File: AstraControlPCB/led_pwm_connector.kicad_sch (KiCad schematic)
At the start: 11 parts, among them CN7 JST_VH_8PIN_10A_250V

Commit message: Update wks file
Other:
- company: (none) -> LiveAstra Technologies
- title: PWM Connector -> AstraControl - Root
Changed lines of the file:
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@@
 	(paper "A4")
 	(title_block
-		(title "PWM Connector")
+		(title "AstraControl - Root")
+		(date "2024-08-26")
+		(rev "A")
+		(company "LiveAstra Technologies")
 	)
 	(junction
@@
 		(effects
 			(font
-				(face "Sarabun")
+				(face "ING Me")
 				(size 3 3)
 				(color 255 255 255 1)
@@
 		(effects
 			(font
-				(face "Sarabun")
+				(face "ING Me")
 				(size 1.5 1.5)
 				(color 255 255 255 1)

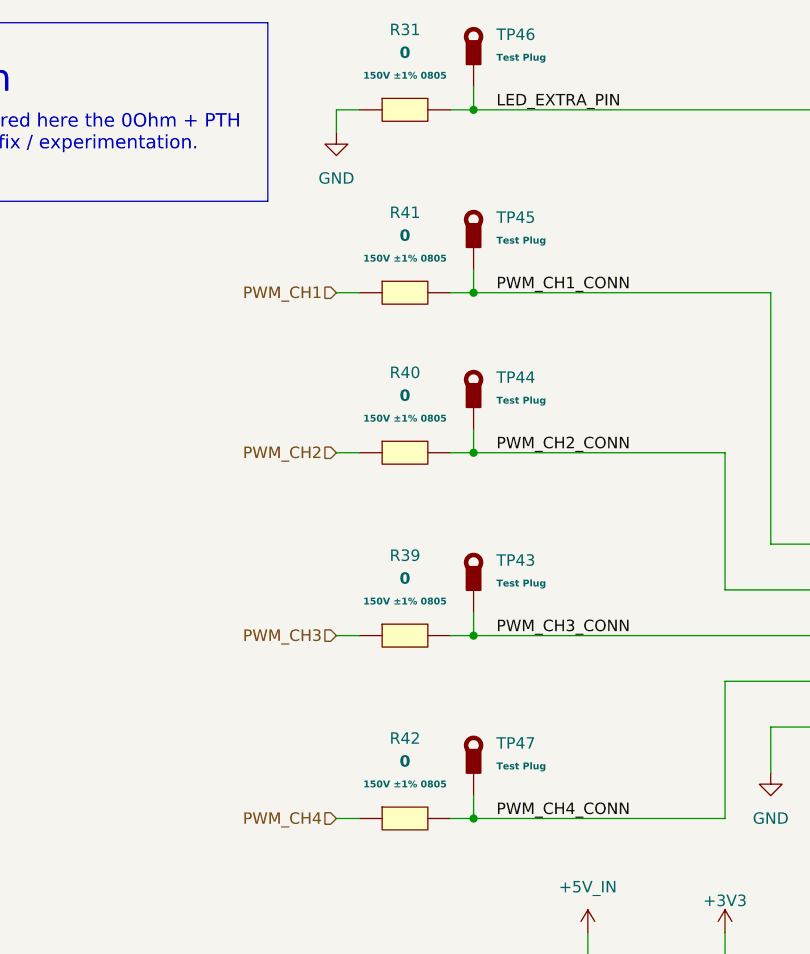
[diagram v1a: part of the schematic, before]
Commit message: Remove plus minus symbol
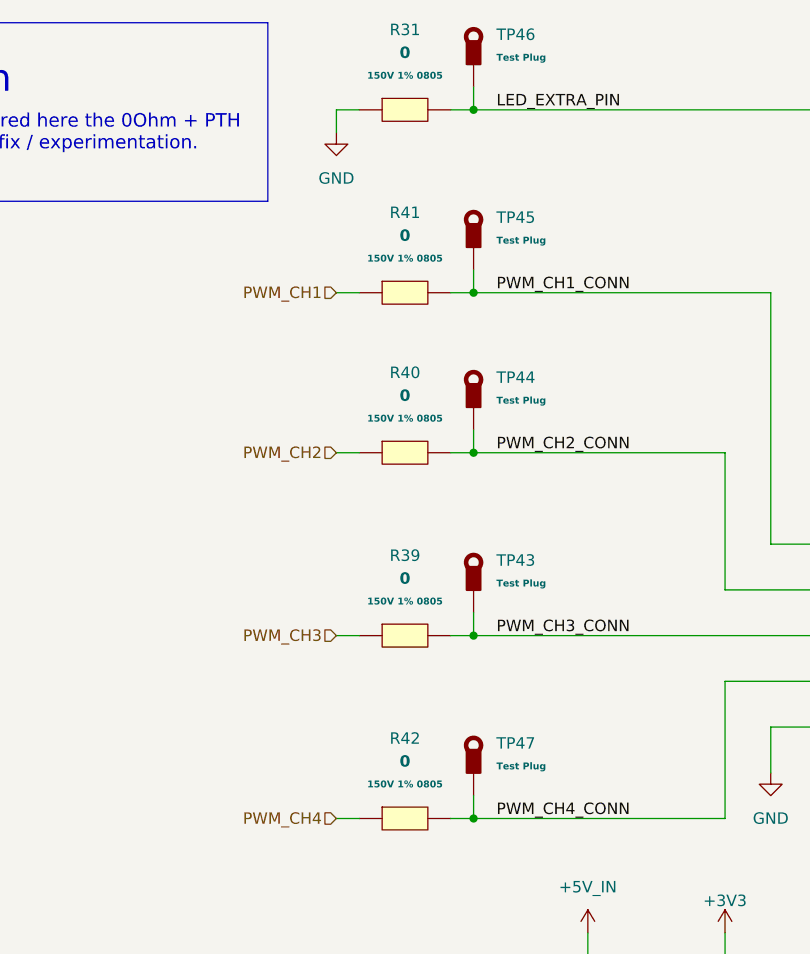
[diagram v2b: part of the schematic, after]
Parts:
- R31, R39, R40, R41, R42: Extra Values 150V ±1% 0805 -> 150V 1% 0805
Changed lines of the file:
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@@
-			)
-		)
-		(property "Extra Value" ""
-			(at 182.88 96.52 0)
-			(effects
-				(font
-					(size 1.27 1.27)
-				)
-				(hide yes)
 			)
 		)
@@
 			)
 		)
-		(property "Extra Value" ""
-			(at 124.46 53.34 0)
-			(effects
-				(font
-					(size 1.27 1.27)
-				)
-				(hide yes)
-			)
-		)
 		(pin "1"
 		)
@@
 		(dnp no)
 		(fields_autoplaced yes)
-		(property "Reference" "#PWR074"
+		(property "Reference" "#PWR74"
 			(at 137.16 130.81 0)
 			(effects
@@
 			(project "AstraControl"
 				(path "/9a751838-dce8-4d69-8a02-736625ac74e7/0db21d8e-3390-4d67-877f-0e5d98e37848/e7f4ae23-1ac9-4fa3-959c-a78f85f3f546"
-					(reference "#PWR074")
+					(reference "#PWR74")
 					(unit 1)
 				)
@@
 		(on_board yes)
 		(dnp no)
-		(property "Reference" "#PWR073"
+		(property "Reference" "#PWR73"
 			(at 152.4 130.81 0)
 			(effects
@@
 			(project "AstraControl"
 				(path "/9a751838-dce8-4d69-8a02-736625ac74e7/0db21d8e-3390-4d67-877f-0e5d98e37848/e7f4ae23-1ac9-4fa3-959c-a78f85f3f546"
-					(reference "#PWR073")
+					(reference "#PWR73")
 					(unit 1)
 				)
@@
 			)
 		)
-		(property "Extra Values" "150V ±1% 0805"
+		(property "Extra Values" "150V 1% 0805"
 			(at 116.84 31.75 0)
 			(effects
@@
 					(bold yes)
 				)
-			)
-		)
-		(property "Extra Value" ""
-			(at 116.84 35.56 0)
-			(effects
-				(font
-					(size 1.27 1.27)
-				)
-				(hide yes)
 			)
 		)
@@
 		(dnp no)
 		(fields_autoplaced yes)
-		(property "Reference" "#PWR075"
+		(property "Reference" "#PWR75"
 			(at 157.48 115.57 0)
 			(effects
@@
 			(project "AstraControl"
 				(path "/9a751838-dce8-4d69-8a02-736625ac74e7/0db21d8e-3390-4d67-877f-0e5d98e37848/e7f4ae23-1ac9-4fa3-959c-a78f85f3f546"
-					(reference "#PWR075")
+					(reference "#PWR75")
 					(unit 1)
 				)
@@
 			)
 		)
-		(property "Extra Values" "150V ±1% 0805"
+		(property "Extra Values" "150V 1% 0805"
 			(at 116.84 69.85 0)
 			(effects
@@
 					(bold yes)
 				)
-			)
-		)
-		(property "Extra Value" ""
-			(at 116.84 73.66 0)
-			(effects
-				(font
-					(size 1.27 1.27)
-				)
-				(hide yes)
 			)
 		)
@@
 			)
 		)
-		(property "Extra Value" ""
-			(at 124.46 71.12 0)
-			(effects
-				(font
-					(size 1.27 1.27)
-				)
-				(hide yes)
-			)
-		)
 		(pin "1"
 		)
@@
 			)
 		)
-		(property "Extra Values" "150V ±1% 0805"
+		(property "Extra Values" "150V 1% 0805"
 			(at 116.84 52.07 0)
 			(effects
@@
 					(bold yes)
 				)
-			)
-		)
-		(property "Extra Value" ""
-			(at 116.84 55.88 0)
-			(effects
-				(font
-					(size 1.27 1.27)
-				)
-				(hide yes)
 			)
 		)
@@
 		(dnp no)
 		(fields_autoplaced yes)
-		(property "Reference" "#PWR072"
+		(property "Reference" "#PWR72"
 			(at 109.22 44.45 0)
 			(effects
@@
 			(project "AstraControl"
 				(path "/9a751838-dce8-4d69-8a02-736625ac74e7/0db21d8e-3390-4d67-877f-0e5d98e37848/e7f4ae23-1ac9-4fa3-959c-a78f85f3f546"
-					(reference "#PWR072")
+					(reference "#PWR72")
 					(unit 1)
 				)
@@
 			)
 		)
-		(property "Extra Value" ""
-			(at 124.46 111.76 0)
-			(effects
-				(font
-					(size 1.27 1.27)
-				)
-				(hide yes)
-			)
-		)
 		(pin "1"
 		)
@@
 			)
 		)
-		(property "Extra Value" ""
-			(at 124.46 91.44 0)
-			(effects
-				(font
-					(size 1.27 1.27)
-				)
-				(hide yes)
-			)
-		)
 		(pin "1"
 		)
@@
 			)
 		)
-		(property "Extra Values" "150V ±1% 0805"
+		(property "Extra Values" "150V 1% 0805"
 			(at 116.84 110.49 0)
 			(effects
@@
 					(bold yes)
 				)
-			)
-		)
-		(property "Extra Value" ""
-			(at 116.84 114.3 0)
-			(effects
-				(font
-					(size 1.27 1.27)
-				)
-				(hide yes)
 			)
 		)
@@
 			)
 		)
-		(property "Extra Values" "150V ±1% 0805"
+		(property "Extra Values" "150V 1% 0805"
 			(at 116.84 90.17 0)
 			(effects
@@
 					(bold yes)
 				)
-			)
-		)
-		(property "Extra Value" ""
-			(at 116.84 93.98 0)
-			(effects
-				(font
-					(size 1.27 1.27)
-				)
-				(hide yes)
 			)
 		)
@@
 			)
 		)
-		(property "Extra Value" ""
-			(at 124.46 33.02 0)
-			(effects
-				(font
-					(size 1.27 1.27)
-				)
-				(hide yes)
-			)
-		)

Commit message: workflow
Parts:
- added INF5: ~, symbol LiveAstra:Information_Box
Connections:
- net LED_EXTRA_PIN renamed EXTRA_PIN
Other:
- note added: "PWM Connector"
- note removed: "If a different signal is required here the 0Ohm + PTH will allow a post assembly fix / experimentation. Otherwise, just GND."
- note removed: "Information"
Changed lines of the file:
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@@
 		)
 	)
-	(rectangle
-		(start 41.7033 25.88)
-		(end 101.6 45.72)
-		(stroke
-			(width 0)
-			(type default)
-		)
-		(fill
-			(type none)
-		)
-	)
-	(text "Information"
-		(exclude_from_sim no)
-		(at 49.2233 32.29 0)
+	(text "PWM Connector"
+		(exclude_from_sim no)
+		(at 19.05 25.4 0)
 		(effects
 			(font
-				(face "ING Me")
-				(size 3 3)
-				(color 255 255 255 1)
-			)
-			(justify left)
-		)
-	)
-	(text "If a different signal is required here the 0Ohm + PTH\nwill allow a post assembly fix / experimentation.\nOtherwise, just GND."
-		(exclude_from_sim no)
-		(at 44.1433 36.1 0)
-		(effects
-			(font
-				(face "ING Me")
-				(size 1.5 1.5)
-				(color 255 255 255 1)
+				(face "ING Me Headline")
+				(size 8 8)
 			)
 			(justify left top)
@@
 		)
 	)
-	(label "LED_EXTRA_PIN"
+	(label "EXTRA_PIN"
 		(at 127 35.56 0)
 		(fields_autoplaced yes)
@@
 		(dnp no)
 		(fields_autoplaced yes)
-		(property "Reference" "#PWR74"
+		(property "Reference" "#PWR074"
 			(at 137.16 130.81 0)
 			(effects
@@
 			(project "AstraControl"
 				(path "/9a751838-dce8-4d69-8a02-736625ac74e7/0db21d8e-3390-4d67-877f-0e5d98e37848/e7f4ae23-1ac9-4fa3-959c-a78f85f3f546"
-					(reference "#PWR74")
+					(reference "#PWR074")
+					(unit 1)
+				)
+			)
+		)
+	)
+	(symbol
+		(lib_id "LiveAstra:Information_Box")
+		(at 190.5 31.75 0)
+		(unit 1)
+		(exclude_from_sim yes)
+		(in_bom no)
+		(on_board no)
+		(dnp no)
+		(fields_autoplaced yes)
+		(property "Reference" "INF5"
+			(at 190.5 20.32 0)
+			(effects
+				(font
+					(size 1.27 1.27)
+				)
+			)
+		)
+		(property "Value" "~"
+			(at 190.5 22.86 0)
+			(effects
+				(font
+					(size 1.27 1.27)
+				)
+			)
+		)
+		(property "Footprint" ""
+			(at 175.26 27.94 0)
+			(effects
+				(font
+					(size 1.27 1.27)
+				)
+				(hide yes)
+			)
+		)
+		(property "Datasheet" ""
+			(at 175.26 27.94 0)
+			(effects
+				(font
+					(size 1.27 1.27)
+				)
+				(hide yes)
+			)
+		)
+		(property "Description" ""
+			(at 175.26 27.94 0)
+			(effects
+				(font
+					(size 1.27 1.27)
+				)
+				(hide yes)
+			)
+		)
+		(instances
+			(project ""
+				(path "/9a751838-dce8-4d69-8a02-736625ac74e7/0db21d8e-3390-4d67-877f-0e5d98e37848/e7f4ae23-1ac9-4fa3-959c-a78f85f3f546"
+					(reference "INF5")
 					(unit 1)
 				)
@@
 		(on_board yes)
 		(dnp no)
-		(property "Reference" "#PWR73"
+		(property "Reference" "#PWR073"
 			(at 152.4 130.81 0)
 			(effects
@@
 			(project "AstraControl"
 				(path "/9a751838-dce8-4d69-8a02-736625ac74e7/0db21d8e-3390-4d67-877f-0e5d98e37848/e7f4ae23-1ac9-4fa3-959c-a78f85f3f546"
-					(reference "#PWR73")
+					(reference "#PWR073")
 					(unit 1)
 				)
@@
 		(dnp no)
 		(fields_autoplaced yes)
-		(property "Reference" "#PWR75"
+		(property "Reference" "#PWR075"
 			(at 157.48 115.57 0)
 			(effects
@@
 			(project "AstraControl"
 				(path "/9a751838-dce8-4d69-8a02-736625ac74e7/0db21d8e-3390-4d67-877f-0e5d98e37848/e7f4ae23-1ac9-4fa3-959c-a78f85f3f546"
-					(reference "#PWR75")
+					(reference "#PWR075")
 					(unit 1)
 				)
@@
 		(dnp no)
 		(fields_autoplaced yes)
-		(property "Reference" "#PWR72"
+		(property "Reference" "#PWR072"
 			(at 109.22 44.45 0)
 			(effects
@@
 			(project "AstraControl"
 				(path "/9a751838-dce8-4d69-8a02-736625ac74e7/0db21d8e-3390-4d67-877f-0e5d98e37848/e7f4ae23-1ac9-4fa3-959c-a78f85f3f546"
-					(reference "#PWR72")
-					(unit 1)
-				)
+					(reference "#PWR072")
+					(unit 1)
+				)

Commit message: update
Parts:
- renumbered INF5 to INF7, R31 to R35, R41 to R36, R40 to R37, R39 to R38, R42 to R39, TP46 to TP39, TP45 to TP40, TP44 to TP41, TP43 to TP42, TP47 to TP43
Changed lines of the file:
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@@
 		(dnp no)
 		(fields_autoplaced yes)
-		(property "Reference" "TP45"
+		(property "Reference" "TP40"
 			(at 127 47.5276 0)
 			(effects
@@
 			(project "AstraControl"
 				(path "/9a751838-dce8-4d69-8a02-736625ac74e7/0db21d8e-3390-4d67-877f-0e5d98e37848/e7f4ae23-1ac9-4fa3-959c-a78f85f3f546"
-					(reference "TP45")
+					(reference "TP40")
 					(unit 1)
 				)
@@
 		(dnp no)
 		(fields_autoplaced yes)
-		(property "Reference" "#PWR074"
+		(property "Reference" "#PWR078"
 			(at 137.16 130.81 0)
 			(effects
@@
 			(project "AstraControl"
 				(path "/9a751838-dce8-4d69-8a02-736625ac74e7/0db21d8e-3390-4d67-877f-0e5d98e37848/e7f4ae23-1ac9-4fa3-959c-a78f85f3f546"
-					(reference "#PWR074")
+					(reference "#PWR078")
 					(unit 1)
 				)
@@
 		(dnp no)
 		(fields_autoplaced yes)
-		(property "Reference" "INF5"
+		(property "Reference" "INF7"
 			(at 190.5 20.32 0)
 			(effects
@@
 			(project ""
 				(path "/9a751838-dce8-4d69-8a02-736625ac74e7/0db21d8e-3390-4d67-877f-0e5d98e37848/e7f4ae23-1ac9-4fa3-959c-a78f85f3f546"
-					(reference "INF5")
+					(reference "INF7")
 					(unit 1)
 				)
@@
 		(on_board yes)
 		(dnp no)
-		(property "Reference" "#PWR073"
+		(property "Reference" "#PWR079"
 			(at 152.4 130.81 0)
 			(effects
@@
 			(project "AstraControl"
 				(path "/9a751838-dce8-4d69-8a02-736625ac74e7/0db21d8e-3390-4d67-877f-0e5d98e37848/e7f4ae23-1ac9-4fa3-959c-a78f85f3f546"
-					(reference "#PWR073")
+					(reference "#PWR079")
 					(unit 1)
 				)
@@
 		(dnp no)
 		(fields_autoplaced yes)
-		(property "Reference" "R31"
+		(property "Reference" "R35"
 			(at 116.84 26.67 0)
 			(effects
@@
 			(project "AstraControl"
 				(path "/9a751838-dce8-4d69-8a02-736625ac74e7/0db21d8e-3390-4d67-877f-0e5d98e37848/e7f4ae23-1ac9-4fa3-959c-a78f85f3f546"
-					(reference "R31")
+					(reference "R35")
 					(unit 1)
 				)
@@
 		(dnp no)
 		(fields_autoplaced yes)
-		(property "Reference" "#PWR075"
+		(property "Reference" "#PWR080"
 			(at 157.48 115.57 0)
 			(effects
@@
 			(project "AstraControl"
 				(path "/9a751838-dce8-4d69-8a02-736625ac74e7/0db21d8e-3390-4d67-877f-0e5d98e37848/e7f4ae23-1ac9-4fa3-959c-a78f85f3f546"
-					(reference "#PWR075")
+					(reference "#PWR080")
 					(unit 1)
 				)
@@
 		(dnp no)
 		(fields_autoplaced yes)
-		(property "Reference" "R40"
+		(property "Reference" "R37"
 			(at 116.84 64.77 0)
 			(effects
@@
 			(project "AstraControl"
 				(path "/9a751838-dce8-4d69-8a02-736625ac74e7/0db21d8e-3390-4d67-877f-0e5d98e37848/e7f4ae23-1ac9-4fa3-959c-a78f85f3f546"
-					(reference "R40")
+					(reference "R37")
 					(unit 1)
 				)
@@
 		(dnp no)
 		(fields_autoplaced yes)
-		(property "Reference" "TP44"
+		(property "Reference" "TP41"
 			(at 127 65.3076 0)
 			(effects
@@
 			(project "AstraControl"
 				(path "/9a751838-dce8-4d69-8a02-736625ac74e7/0db21d8e-3390-4d67-877f-0e5d98e37848/e7f4ae23-1ac9-4fa3-959c-a78f85f3f546"
-					(reference "TP44")
+					(reference "TP41")
 					(unit 1)
 				)
@@
 		(dnp no)
 		(fields_autoplaced yes)
-		(property "Reference" "R41"
+		(property "Reference" "R36"
 			(at 116.84 46.99 0)
 			(effects
@@
 			(project "AstraControl"
 				(path "/9a751838-dce8-4d69-8a02-736625ac74e7/0db21d8e-3390-4d67-877f-0e5d98e37848/e7f4ae23-1ac9-4fa3-959c-a78f85f3f546"
-					(reference "R41")
+					(reference "R36")
 					(unit 1)
 				)
@@
 		(dnp no)
 		(fields_autoplaced yes)
-		(property "Reference" "#PWR072"
+		(property "Reference" "#PWR077"
 			(at 109.22 44.45 0)
 			(effects
@@
 			(project "AstraControl"
 				(path "/9a751838-dce8-4d69-8a02-736625ac74e7/0db21d8e-3390-4d67-877f-0e5d98e37848/e7f4ae23-1ac9-4fa3-959c-a78f85f3f546"
-					(reference "#PWR072")
+					(reference "#PWR077")
 					(unit 1)
 				)
@@
 		(dnp no)
 		(fields_autoplaced yes)
-		(property "Reference" "TP47"
+		(property "Reference" "TP43"
 			(at 127 105.9476 0)
 			(effects
@@
 			(project "AstraControl"
 				(path "/9a751838-dce8-4d69-8a02-736625ac74e7/0db21d8e-3390-4d67-877f-0e5d98e37848/e7f4ae23-1ac9-4fa3-959c-a78f85f3f546"
-					(reference "TP47")
+					(reference "TP43")
 					(unit 1)
 				)
@@
 		(dnp no)
 		(fields_autoplaced yes)
-		(property "Reference" "TP43"
+		(property "Reference" "TP42"
 			(at 127 85.6276 0)
 			(effects
@@
 			(project "AstraControl"
 				(path "/9a751838-dce8-4d69-8a02-736625ac74e7/0db21d8e-3390-4d67-877f-0e5d98e37848/e7f4ae23-1ac9-4fa3-959c-a78f85f3f546"
-					(reference "TP43")
+					(reference "TP42")
 					(unit 1)
 				)
@@
 		(dnp no)
 		(fields_autoplaced yes)
-		(property "Reference" "R42"
+		(property "Reference" "R39"
 			(at 116.84 105.41 0)
 			(effects
@@
 			(project "AstraControl"
 				(path "/9a751838-dce8-4d69-8a02-736625ac74e7/0db21d8e-3390-4d67-877f-0e5d98e37848/e7f4ae23-1ac9-4fa3-959c-a78f85f3f546"
-					(reference "R42")
+					(reference "R39")
 					(unit 1)
 				)
@@
 		(dnp no)
 		(fields_autoplaced yes)
-		(property "Reference" "R39"
+		(property "Reference" "R38"
 			(at 116.84 85.09 0)
 			(effects
@@
 			(project "AstraControl"
 				(path "/9a751838-dce8-4d69-8a02-736625ac74e7/0db21d8e-3390-4d67-877f-0e5d98e37848/e7f4ae23-1ac9-4fa3-959c-a78f85f3f546"
-					(reference "R39")
+					(reference "R38")
 					(unit 1)
 				)
@@
 		(dnp no)
 		(fields_autoplaced yes)
-		(property "Reference" "TP46"
+		(property "Reference" "TP39"
 			(at 127 27.2076 0)
 			(effects
@@
 			(project "AstraControl"
 				(path "/9a751838-dce8-4d69-8a02-736625ac74e7/0db21d8e-3390-4d67-877f-0e5d98e37848/e7f4ae23-1ac9-4fa3-959c-a78f85f3f546"
-					(reference "TP46")
-					(unit 1)
-				)
+					(reference "TP39")
+					(unit 1)
+				)

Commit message: update
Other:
- note added: "If a different signal is required here the 0Ohm + PTH will allow a post assembly fix / experimentation. Otherwise, just GND."

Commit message: update
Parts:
- removed INF7: ~, symbol LiveAstra:Information_Box
- added INF7: ~, symbol LiveAstra:Information_Box_XL

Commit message: Updates
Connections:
- net EXTRA_PIN renamed RESERVED_PIN
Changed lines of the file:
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@@
 		)
 	)
-	(label "EXTRA_PIN"
+	(label "RESERVED_PIN"
 		(at 127 35.56 0)
 		(fields_autoplaced yes)

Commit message: Updates
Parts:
- renumbered INF7 to INF9, R35 to R36, R36 to R37, R37 to R38, R38 to R39, R39 to R40
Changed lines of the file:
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@@
 			)
 		)
-		(property "Datasheet" ""
+		(property "Datasheet" "https://www.lcsc.com/product-detail/Thimble-Copper-Rod-Test-Ring_ronghe-RH-5000_C5277086.html"
 			(at 124.46 48.26 90)
 			(effects
@@
 		(dnp no)
 		(fields_autoplaced yes)
-		(property "Reference" "#PWR078"
+		(property "Reference" "#PWR080"
 			(at 137.16 130.81 0)
 			(effects
@@
 			(project "AstraControl"
 				(path "/9a751838-dce8-4d69-8a02-736625ac74e7/0db21d8e-3390-4d67-877f-0e5d98e37848/e7f4ae23-1ac9-4fa3-959c-a78f85f3f546"
-					(reference "#PWR078")
+					(reference "#PWR080")
 					(unit 1)
 				)
@@
 		(on_board yes)
 		(dnp no)
-		(property "Reference" "#PWR079"
+		(property "Reference" "#PWR081"
 			(at 152.4 130.81 0)
 			(effects
@@
 			(project "AstraControl"
 				(path "/9a751838-dce8-4d69-8a02-736625ac74e7/0db21d8e-3390-4d67-877f-0e5d98e37848/e7f4ae23-1ac9-4fa3-959c-a78f85f3f546"
-					(reference "#PWR079")
+					(reference "#PWR081")
 					(unit 1)
 				)
@@
 		(dnp no)
 		(fields_autoplaced yes)
-		(property "Reference" "R35"
+		(property "Reference" "R36"
 			(at 116.84 26.67 0)
 			(effects
@@
 			(project "AstraControl"
 				(path "/9a751838-dce8-4d69-8a02-736625ac74e7/0db21d8e-3390-4d67-877f-0e5d98e37848/e7f4ae23-1ac9-4fa3-959c-a78f85f3f546"
-					(reference "R35")
+					(reference "R36")
 					(unit 1)
 				)
@@
 		(dnp no)
 		(fields_autoplaced yes)
-		(property "Reference" "#PWR080"
+		(property "Reference" "#PWR082"
 			(at 157.48 115.57 0)
 			(effects
@@
 			(project "AstraControl"
 				(path "/9a751838-dce8-4d69-8a02-736625ac74e7/0db21d8e-3390-4d67-877f-0e5d98e37848/e7f4ae23-1ac9-4fa3-959c-a78f85f3f546"
-					(reference "#PWR080")
+					(reference "#PWR082")
 					(unit 1)
 				)
@@
 		(dnp no)
 		(fields_autoplaced yes)
-		(property "Reference" "R37"
+		(property "Reference" "R38"
 			(at 116.84 64.77 0)
 			(effects
@@
 			(project "AstraControl"
 				(path "/9a751838-dce8-4d69-8a02-736625ac74e7/0db21d8e-3390-4d67-877f-0e5d98e37848/e7f4ae23-1ac9-4fa3-959c-a78f85f3f546"
-					(reference "R37")
+					(reference "R38")
 					(unit 1)
 				)
@@
 			)
 		)
-		(property "Datasheet" ""
+		(property "Datasheet" "https://www.lcsc.com/product-detail/Thimble-Copper-Rod-Test-Ring_ronghe-RH-5000_C5277086.html"
 			(at 124.46 66.04 90)
 			(effects
@@
 		(dnp no)
 		(fields_autoplaced yes)
-		(property "Reference" "R36"
+		(property "Reference" "R37"
 			(at 116.84 46.99 0)
 			(effects
@@
 			(project "AstraControl"
 				(path "/9a751838-dce8-4d69-8a02-736625ac74e7/0db21d8e-3390-4d67-877f-0e5d98e37848/e7f4ae23-1ac9-4fa3-959c-a78f85f3f546"
-					(reference "R36")
+					(reference "R37")
 					(unit 1)
 				)
@@
 		(dnp no)
 		(fields_autoplaced yes)
-		(property "Reference" "INF7"
+		(property "Reference" "INF9"
 			(at 219.71 34.9249 0)
 			(effects
@@
 			(project ""
 				(path "/9a751838-dce8-4d69-8a02-736625ac74e7/0db21d8e-3390-4d67-877f-0e5d98e37848/e7f4ae23-1ac9-4fa3-959c-a78f85f3f546"
-					(reference "INF7")
+					(reference "INF9")
 					(unit 1)
 				)
@@
 		(dnp no)
 		(fields_autoplaced yes)
-		(property "Reference" "#PWR077"
+		(property "Reference" "#PWR079"
 			(at 109.22 44.45 0)
 			(effects
@@
 			(project "AstraControl"
 				(path "/9a751838-dce8-4d69-8a02-736625ac74e7/0db21d8e-3390-4d67-877f-0e5d98e37848/e7f4ae23-1ac9-4fa3-959c-a78f85f3f546"
-					(reference "#PWR077")
+					(reference "#PWR079")
 					(unit 1)
 				)
@@
 			)
 		)
-		(property "Datasheet" ""
+		(property "Datasheet" "https://www.lcsc.com/product-detail/Thimble-Copper-Rod-Test-Ring_ronghe-RH-5000_C5277086.html"
 			(at 124.46 106.68 90)
 			(effects
@@
 			)
 		)
-		(property "Datasheet" ""
+		(property "Datasheet" "https://www.lcsc.com/product-detail/Thimble-Copper-Rod-Test-Ring_ronghe-RH-5000_C5277086.html"
 			(at 124.46 86.36 90)
 			(effects
@@
 		(dnp no)
 		(fields_autoplaced yes)
-		(property "Reference" "R39"
+		(property "Reference" "R40"
 			(at 116.84 105.41 0)
 			(effects
@@
 			(project "AstraControl"
 				(path "/9a751838-dce8-4d69-8a02-736625ac74e7/0db21d8e-3390-4d67-877f-0e5d98e37848/e7f4ae23-1ac9-4fa3-959c-a78f85f3f546"
-					(reference "R39")
+					(reference "R40")
 					(unit 1)
 				)
@@
 		(dnp no)
 		(fields_autoplaced yes)
-		(property "Reference" "R38"
+		(property "Reference" "R39"
 			(at 116.84 85.09 0)
 			(effects
@@
 			(project "AstraControl"
 				(path "/9a751838-dce8-4d69-8a02-736625ac74e7/0db21d8e-3390-4d67-877f-0e5d98e37848/e7f4ae23-1ac9-4fa3-959c-a78f85f3f546"
-					(reference "R38")
+					(reference "R39")
 					(unit 1)
 				)
@@
 			)
 		)
-		(property "Datasheet" ""
+		(property "Datasheet" "https://www.lcsc.com/product-detail/Thimble-Copper-Rod-Test-Ring_ronghe-RH-5000_C5277086.html"
 			(at 124.46 27.94 90)
 			(effects
